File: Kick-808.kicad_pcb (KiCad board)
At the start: 2 copper layers, 19.3 x 106.5 mm, 70 parts, among them J3 Conn_02x05_Odd_Even, Q1 BC847, Q2 BC847, Q3 BC857, Q4 BC847, Q5 BC847, Q6 BC847, Q7 BC847, SW1 SW_Push_LED, U1 TL072, U2 TL072

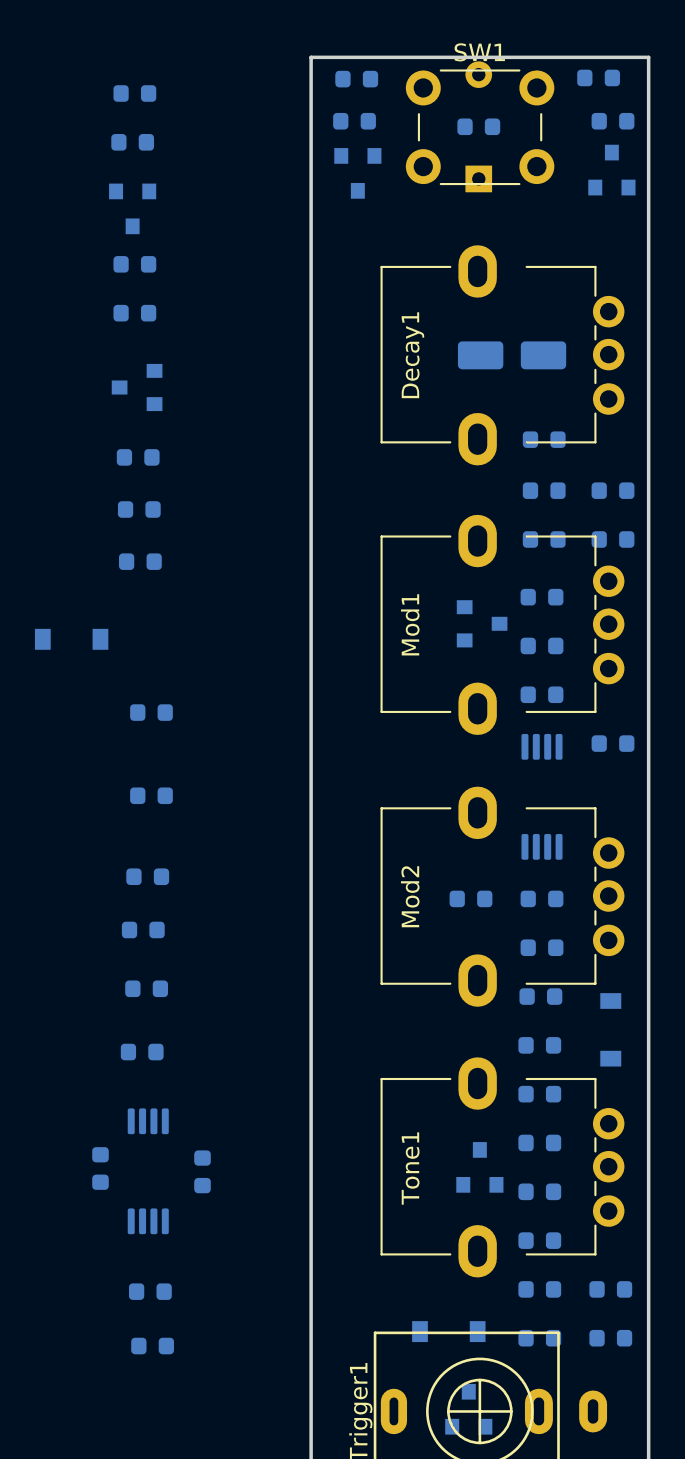
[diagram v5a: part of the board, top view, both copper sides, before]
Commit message: Initial placement on rear right-side.
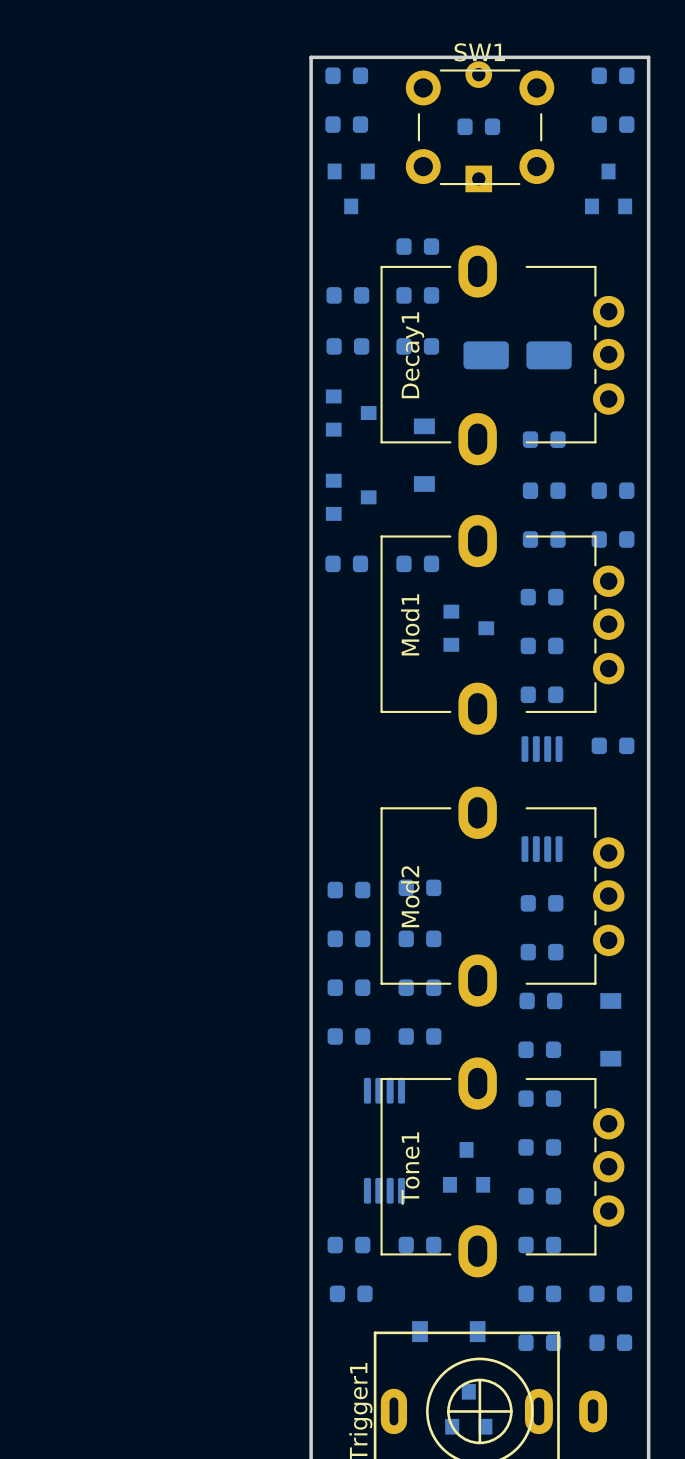
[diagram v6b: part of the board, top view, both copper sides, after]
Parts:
- moved R7 31.4 mm to (123.4, 77.3)
- moved R8 27.1 mm to (119.4, 77.3), turned to 0 degrees
- moved D2 22.8 mm to (123.8, 71.1), turned to 90 degrees
- moved Q1 20.7 mm to (119.6, 73.5), turned to 0 degrees
- moved C8 20.1 mm to (123.4, 62.0)
- moved R18 20.1 mm to (123.4, 64.9)
- moved R15 20.0 mm to (123.4, 59.2), turned to 0 degrees
- moved C11 16.4 mm to (123.6, 116.3)
- moved R4 16.2 mm to (123.6, 101.6), turned to 0 degrees
- moved R3 16.0 mm to (123.6, 98.8), turned to 0 degrees
- moved R2 15.2 mm to (119.5, 96.0), turned to 180 degrees
- moved C14 14.9 mm to (119.5, 116.3), turned to 0 degrees
- moved C15 14.7 mm to (123.6, 104.4), turned to 0 degrees
- moved R1 14.0 mm to (119.5, 98.8), turned to 0 degrees
- moved U1 13.6 mm to (121.5, 110.4)
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
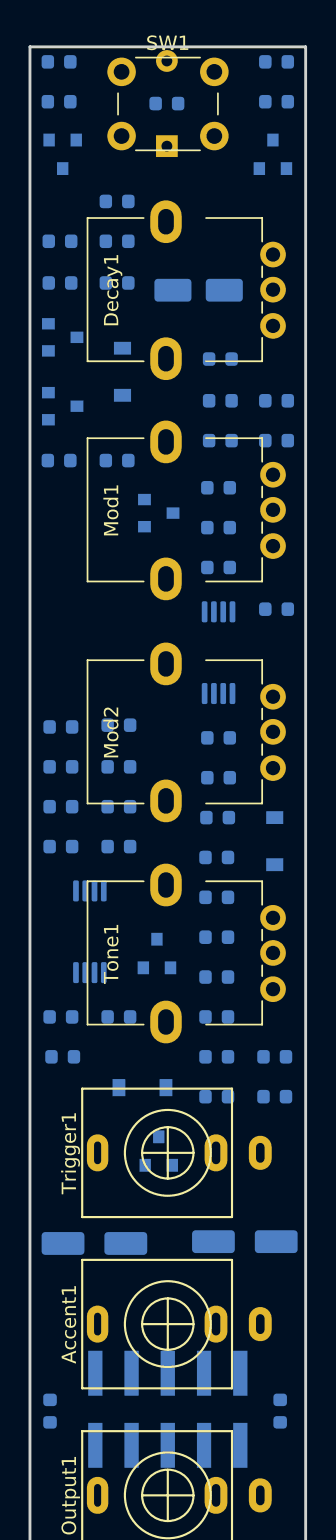
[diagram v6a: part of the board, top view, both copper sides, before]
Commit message: Basic power routing.
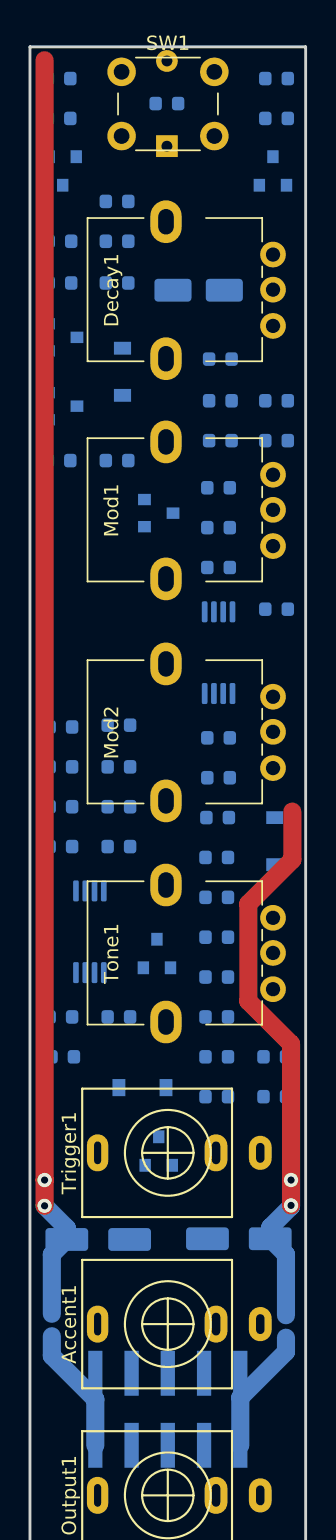
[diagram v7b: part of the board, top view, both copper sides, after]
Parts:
- moved FB1 6.03 mm to (118.9, 137.9)
- moved FB2 5.94 mm to (135.3, 138.0)
- moved Q6 1.17 mm to (134.4, 57.0)
- moved Q7 1.17 mm to (119.6, 57.0)
- moved R26 1.17 mm to (134.6, 53.4)
- moved R28 1.17 mm to (134.6, 50.6)
- moved R31 1.17 mm to (119.4, 53.4)
- moved R32 1.17 mm to (119.4, 50.6)
- moved C4 0.47 mm to (132.0, 131.9)
- moved C3 0.39 mm to (122.1, 131.9)
- turned C5 to 180 degrees
- turned R16 to 180 degrees
- turned R23 to 0 degrees
- turned R3 to 180 degrees
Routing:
- net +12V: track 0.00 -> 88.9 mm, vias 0 -> 2
- net -12V: track 0.00 -> 40.7 mm, vias 0 -> 2
- net Net-(FB1-Pad2): track 0.00 -> 8.91 mm
- net Net-(FB2-Pad2): track 0.00 -> 8.87 mm

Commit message: Ground pour on front.
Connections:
- Accent1 pad S: (no net) -> GND
- C11 pad 2: (no net) -> GND
- C12 pad 2: (no net) -> GND
- C14 pad 1: (no net) -> GND
- C15 pad 2: (no net) -> GND
- C2 pad 2: (no net) -> GND
- C3 pad 2: (no net) -> GND
- C4 pad 1: (no net) -> GND
- C6 pad 1: (no net) -> GND
- C7 pad 2: (no net) -> GND
- D2 pad 1: (no net) -> GND
- D3 pad 2: (no net) -> GND
- J3 pad 3: (no net) -> GND
- J3 pad 4: (no net) -> GND
- J3 pad 5: (no net) -> GND
- J3 pad 6: (no net) -> GND
- J3 pad 7: (no net) -> GND
- J3 pad 8: (no net) -> GND
- Mod2 pad 2: (no net) -> GND
- Mod2 pad 3: (no net) -> GND
- Output1 pad S: (no net) -> GND
- Q1 pad 2: (no net) -> GND
- Q2 pad 2: (no net) -> GND
- Q4 pad 2: (no net) -> GND
- Q5 pad 2: (no net) -> GND
- Q7 pad 2: (no net) -> GND
- R10 pad 2: (no net) -> GND
- R17 pad 2: (no net) -> GND
- R2 pad 2: (no net) -> GND
- R27 pad 2: (no net) -> GND
- R5 pad 2: (no net) -> GND
- R6 pad 2: (no net) -> GND
- R8 pad 1: (no net) -> GND
- Trigger1 pad S: (no net) -> GND
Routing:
- added copper zone on F.Cu, net GND
